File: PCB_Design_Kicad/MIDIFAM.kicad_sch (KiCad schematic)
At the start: 44 parts, among them IC1 DAC8562SDGSR, J1 PWR_IN, J10 midi, J2 ISP connector, U1 TL072, U2 MCP1703Ax-500xxDB, U5 6N137, U6 ATmega328-A

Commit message: better routing
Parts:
- added J11: back bottom, Connector_PinHeader_2.54mm:PinHeader_1x11_P2.54mm_Vertical, symbol Connector_Generic:Conn_01x11
- added J13: back top, Connector_PinHeader_2.54mm:PinHeader_1x07_P2.54mm_Vertical, symbol Connector_Generic:Conn_01x07
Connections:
- net GND: now also J11.11 (Pin_11), J13.7 (Pin_7)
- net adv_clock_b: now also J13.4 (Pin_4)
- net learn_sw_b: now also J11.5 (Pin_5)
- net led_a1_b: now also J11.7 (Pin_7)
- net led_a2_b: now also J11.8 (Pin_8)
- net led_b1_b: now also J11.4 (Pin_4)
- net led_b2_b: now also J11.3 (Pin_3)
- net led_cl1_b: now also J11.10 (Pin_10)
- net led_cl2_b: now also J11.9 (Pin_9)
- net seq_mode_sw_b: now also J13.3 (Pin_3)
- net sync_sw_b: now also J11.6 (Pin_6)
- net trig_a_b: now also J11.2 (Pin_2)
- net trig_b_b: now also J11.1 (Pin_1)
- net vel_a_b: now also J13.2 (Pin_2)
- net vel_b_b: now also J13.1 (Pin_1)
- net voct_a_b: now also J13.5 (Pin_5)
- net voct_b_b: now also J13.6 (Pin_6)
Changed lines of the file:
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@@
 	)
 	(label "led_cl2_b"
-		(at 116.84 78.74 180)
+		(at 121.92 58.42 180)
 		(fields_autoplaced yes)
 		(effects
@@
 	)
 	(label "trig_b_b"
-		(at 116.84 50.165 180)
+		(at 121.92 38.1 180)
 		(fields_autoplaced yes)
 		(effects
@@
 	)
 	(label "seq_mode_sw_b"
-		(at 116.84 81.28 180)
+		(at 121.92 81.915 180)
 		(fields_autoplaced yes)
 		(effects
@@
 	)
 	(label "learn_sw_b"
-		(at 116.84 31.75 180)
+		(at 121.92 48.26 180)
 		(fields_autoplaced yes)
 		(effects
@@
 	)
 	(label "sync_sw_b"
-		(at 116.84 29.21 180)
+		(at 121.92 50.8 180)
 		(fields_autoplaced yes)
 		(effects
@@
 	)
 	(label "led_a1_b"
-		(at 116.84 26.67 180)
+		(at 121.92 53.34 180)
 		(fields_autoplaced yes)
 		(effects
@@
 	)
 	(label "adv_clock_b"
-		(at 116.84 83.82 180)
+		(at 121.92 84.455 180)
 		(fields_autoplaced yes)
 		(effects
@@
 	)
 	(label "voct_b_b"
-		(at 116.84 55.245 180)
+		(at 121.92 89.535 180)
 		(fields_autoplaced yes)
 		(effects
@@
 	)
 	(label "led_b2_b"
-		(at 116.84 36.83 180)
+		(at 121.92 43.18 180)
 		(fields_autoplaced yes)
 		(effects
@@
 	)
 	(label "vel_b_b"
-		(at 116.84 62.865 180)
+		(at 121.92 76.835 180)
 		(fields_autoplaced yes)
 		(effects
@@
 	)
 	(label "trig_a_b"
-		(at 116.84 52.705 180)
+		(at 121.92 40.64 180)
 		(fields_autoplaced yes)
 		(effects
@@
 	)
 	(label "led_a2_b"
-		(at 116.84 24.13 180)
+		(at 121.92 55.88 180)
 		(fields_autoplaced yes)
 		(effects
@@
 	)
 	(label "vel_a_b"
-		(at 116.84 60.325 180)
+		(at 121.92 79.375 180)
 		(fields_autoplaced yes)
 		(effects
@@
 	)
 	(label "voct_a_b"
-		(at 116.84 57.785 180)
+		(at 121.92 86.995 180)
 		(fields_autoplaced yes)
 		(effects
@@
 	)
 	(label "led_b1_b"
-		(at 116.84 34.29 180)
+		(at 121.92 45.72 180)
 		(fields_autoplaced yes)
 		(effects
@@
 	)
 	(label "led_cl1_b"
-		(at 116.84 76.2 180)
+		(at 121.92 60.96 180)
 		(fields_autoplaced yes)
 		(effects
@@
 	(symbol
 		(lib_id "power:GND")
-		(at 116.84 65.405 0)
+		(at 121.92 92.075 0)
 		(unit 1)
 		(exclude_from_sim no)
@@
 		(dnp no)
 		(property "Reference" "#PWR033"
-			(at 116.84 71.755 0)
+			(at 121.92 98.425 0)
 			(effects
 				(font
@@
 		)
 		(property "Value" "GND"
-			(at 116.84 69.215 0)
+			(at 121.92 95.885 0)
 			(effects
 				(font
@@
 		)
 		(property "Footprint" ""
-			(at 116.84 65.405 0)
+			(at 121.92 92.075 0)
 			(effects
 				(font
@@
 		)
 		(property "Datasheet" ""
-			(at 116.84 65.405 0)
+			(at 121.92 92.075 0)
 			(effects
 				(font
@@
 		)
 		(property "Description" "Power symbol creates a global label with name \"GND\" , ground"
-			(at 116.84 65.405 0)
+			(at 121.92 92.075 0)
 			(effects
 				(font
@@
 	)
 	(symbol
+		(lib_id "Connector_Generic:Conn_01x07")
+		(at 127 84.455 0)
+		(unit 1)
+		(exclude_from_sim no)
+		(in_bom yes)
+		(on_board yes)
+		(dnp no)
+		(fields_autoplaced yes)
+		(property "Reference" "J13"
+			(at 129.54 83.1849 0)
+			(effects
+				(font
+					(size 1.27 1.27)
+				)
+				(justify left)
+			)
+		)
+		(property "Value" "back top"
+			(at 129.54 85.7249 0)
+			(effects
+				(font
+					(size 1.27 1.27)
+				)
+				(justify left)
+			)
+		)
+		(property "Footprint" "Connector_PinHeader_2.54mm:PinHeader_1x07_P2.54mm_Vertical"
+			(at 127 84.455 0)
+			(effects
+				(font
+					(size 1.27 1.27)
+				)
+				(hide yes)
+			)
+		)
+		(property "Datasheet" "~"
+			(at 127 84.455 0)
+			(effects
+				(font
+					(size 1.27 1.27)
+				)
+				(hide yes)
+			)
+		)
+		(property "Description" "Generic connector, single row, 01x07, script generated (kicad-library-utils/schlib/autogen/connector/)"
+			(at 127 84.455 0)
+			(effects
+				(font
+					(size 1.27 1.27)
+				)
+				(hide yes)
+			)
+		)
+		(pin "2"
+		)
+		(pin "1"
+		)
+		(pin "3"
+		)
+		(pin "6"
+		)
+		(pin "4"
+		)
+		(pin "5"
+		)
+		(pin "7"
+		)
+		(instances
+			(project ""
+				(path "/4d4d84f1-a7a8-42a8-95d1-cf69d5b591e2"
+					(reference "J13")
+					(unit 1)
+				)
+			)
+		)
+	)
+	(symbol
 		(lib_id "power:GND")
 		(at 208.28 144.78 0)
@@
 	)
 	(symbol
+		(lib_id "Connector_Generic:Conn_01x11")
+		(at 127 50.8 0)
+		(unit 1)
+		(exclude_from_sim no)
+		(in_bom yes)
+		(on_board yes)
+		(dnp no)
+		(fields_autoplaced yes)
+		(property "Reference" "J11"
+			(at 129.54 49.5299 0)
+			(effects
+				(font
+					(size 1.27 1.27)
+				)
+				(justify left)
+			)
+		)
+		(property "Value" "back bottom"
+			(at 129.54 52.0699 0)
+			(effects
+				(font
+					(size 1.27 1.27)
+				)
+				(justify left)
+			)
+		)
+		(property "Footprint" "Connector_PinHeader_2.54mm:PinHeader_1x11_P2.54mm_Vertical"
+			(at 127 50.8 0)
+			(effects
+				(font
+					(size 1.27 1.27)
+				)
+				(hide yes)
+			)
+		)
+		(property "Datasheet" "~"
+			(at 127 50.8 0)
+			(effects
+				(font
+					(size 1.27 1.27)
+				)
+				(hide yes)
+			)
+		)
+		(property "Description" "Generic connector, single row, 01x11, script generated (kicad-library-utils/schlib/autogen/connector/)"
+			(at 127 50.8 0)
+			(effects
+				(font
+					(size 1.27 1.27)
+				)
+				(hide yes)
+			)
+		)
+		(pin "6"
+		)
+		(pin "10"
+		)
+		(pin "9"
+		)
+		(pin "1"
+		)
+		(pin "5"
+		)
+		(pin "8"
+		)
+		(pin "11"
+		)
+		(pin "3"
+		)
+		(pin "7"
+		)
+		(pin "2"
+		)
+		(pin "4"
+		)
+		(instances
+			(project ""
+				(path "/4d4d84f1-a7a8-42a8-95d1-cf69d5b591e2"
+					(reference "J11")
+					(unit 1)
+				)
+			)
+		)
+	)
+	(symbol
 		(lib_id "Regulator_Linear:MCP1703Ax-500xxDB")
 		(at 92.075 173.355 270)
@@
 	(symbol
 		(lib_id "power:GND")
-		(at 116.84 39.37 0)
+		(at 121.92 63.5 0)
 		(unit 1)
 		(exclude_from_sim no)
@@
 		(dnp no)
 		(property "Reference" "#PWR034"
-			(at 116.84 45.72 0)
+			(at 121.92 69.85 0)
 			(effects
 				(font
@@
 		)
 		(property "Value" "GND"
-			(at 116.84 43.18 0)
+			(at 121.92 67.31 0)
 			(effects
 				(font
@@
 		)
 		(property "Footprint" ""
-			(at 116.84 39.37 0)
+			(at 121.92 63.5 0)
 			(effects
 				(font
@@
 		)
 		(property "Datasheet" ""
-			(at 116.84 39.37 0)
+			(at 121.92 63.5 0)
 			(effects
 				(font
@@
 		)
 		(property "Description" "Power symbol creates a global label with name \"GND\" , ground"
-			(at 116.84 39.37 0)
+			(at 121.92 63.5 0)
 			(effects
 				(font
@@
 					(unit 1)
 				)
-			)
-		)
-	)
-	(symbol
-		(lib_id "power:GND")
-		(at 116.84 86.36 0)
-		(unit 1)
-		(exclude_from_sim no)
-		(in_bom yes)
-		(on_board yes)
-		(dnp no)
-		(property "Reference" "#PWR032"
-			(at 116.84 92.71 0)
-			(effects
-				(font
-					(size 1.27 1.27)
-				)
-				(hide yes)
-			)
-		)
-		(property "Value" "GND"
-			(at 116.84 90.17 0)
-			(effects
-				(font
-					(size 1.27 1.27)
-				)
-			)
-		)
-		(property "Footprint" ""
-			(at 116.84 86.36 0)
-			(effects
-				(font
-					(size 1.27 1.27)
-				)
-				(hide yes)
-			)
-		)
-		(property "Datasheet" ""
-			(at 116.84 86.36 0)
-			(effects
-				(font
-					(size 1.27 1.27)
-				)
-				(hide yes)
-			)
-		)
-		(property "Description" "Power symbol creates a global label with name \"GND\" , ground"
-			(at 116.84 86.36 0)
-			(effects
-				(font
-					(size 1.27 1.27)
-				)
-				(hide yes)
-			)
-		)
-		(pin "1"
-		)
-		(instances
-			(project "MIDIFAM"
-				(path "/4d4d84f1-a7a8-42a8-95d1-cf69d5b591e2"
-					(reference "#PWR032")
-					(unit 1)
-				)

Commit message: ready for schematic review
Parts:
- removed C4, C5: 1u, Capacitor_SMD:C_0603_1608Metric, symbol Device:C_Polarized_Small
- added C18, C19: 18p, Capacitor_SMD:C_0603_1608Metric, symbol Device:C_Small
- added D7: 1N4148, Diode_SMD:D_SOD-323_HandSoldering, symbol Device:D_Small
- added R16, R17: 47k, Resistor_SMD:R_0603_1608Metric_Pad0.98x0.95mm_HandSolder, symbol Device:R_Small
- added R18, R19: 1k, Resistor_SMD:R_0603_1608Metric_Pad0.98x0.95mm_HandSolder, symbol Device:R_Small
- R1, R3: value ? -> 240k
- R2, R4: value ? -> 47k
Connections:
- net 5V: now also D7.1 (K)
- net DAC_OUT_A: now also R2.2; no longer U1.5 (+)
- net DAC_OUT_B: now also R4.2; no longer U1.3 (+)
- net GND: now also R17.1; no longer R2.1, R4.1
- net RESET: now also D7.2 (A)
- net VREF_DAC: now also R16.2
- net voct_a_b: now also R1.1, R18.1; no longer R1.2, U1.7
- net voct_b_b: now also R3.1, R19.1; no longer R3.2, U1.1
- new net: C19.1, R3.2, R4.1, U1.2 (-)
- new net: C18.2, R18.2, U1.7
- new net: C18.1, R1.2, R2.1, U1.6 (-)
- new net: C19.2, R19.2, U1.1
- new net VREF/2: R16.1, R17.2, U1.3 (+), U1.5 (+)
- no-connect marks 4 -> 6
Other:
- moved on the sheet: C17, IC1, R10, R11, R12, R13, R14, U1A, U1B

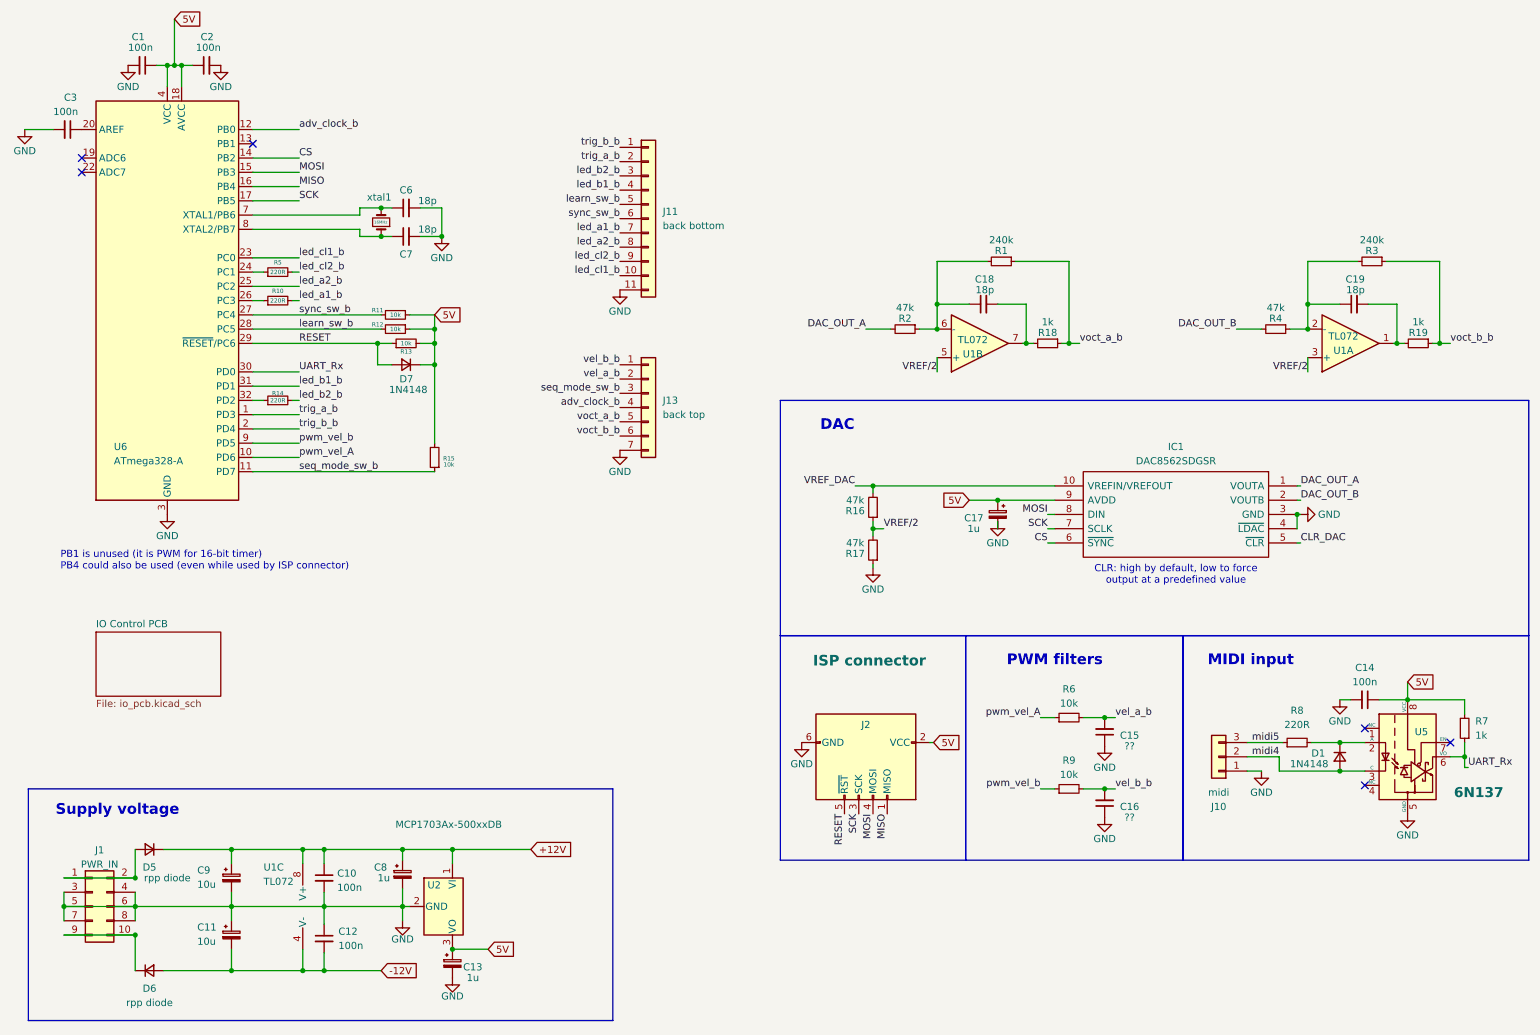
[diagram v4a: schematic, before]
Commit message: op amps for velocity!
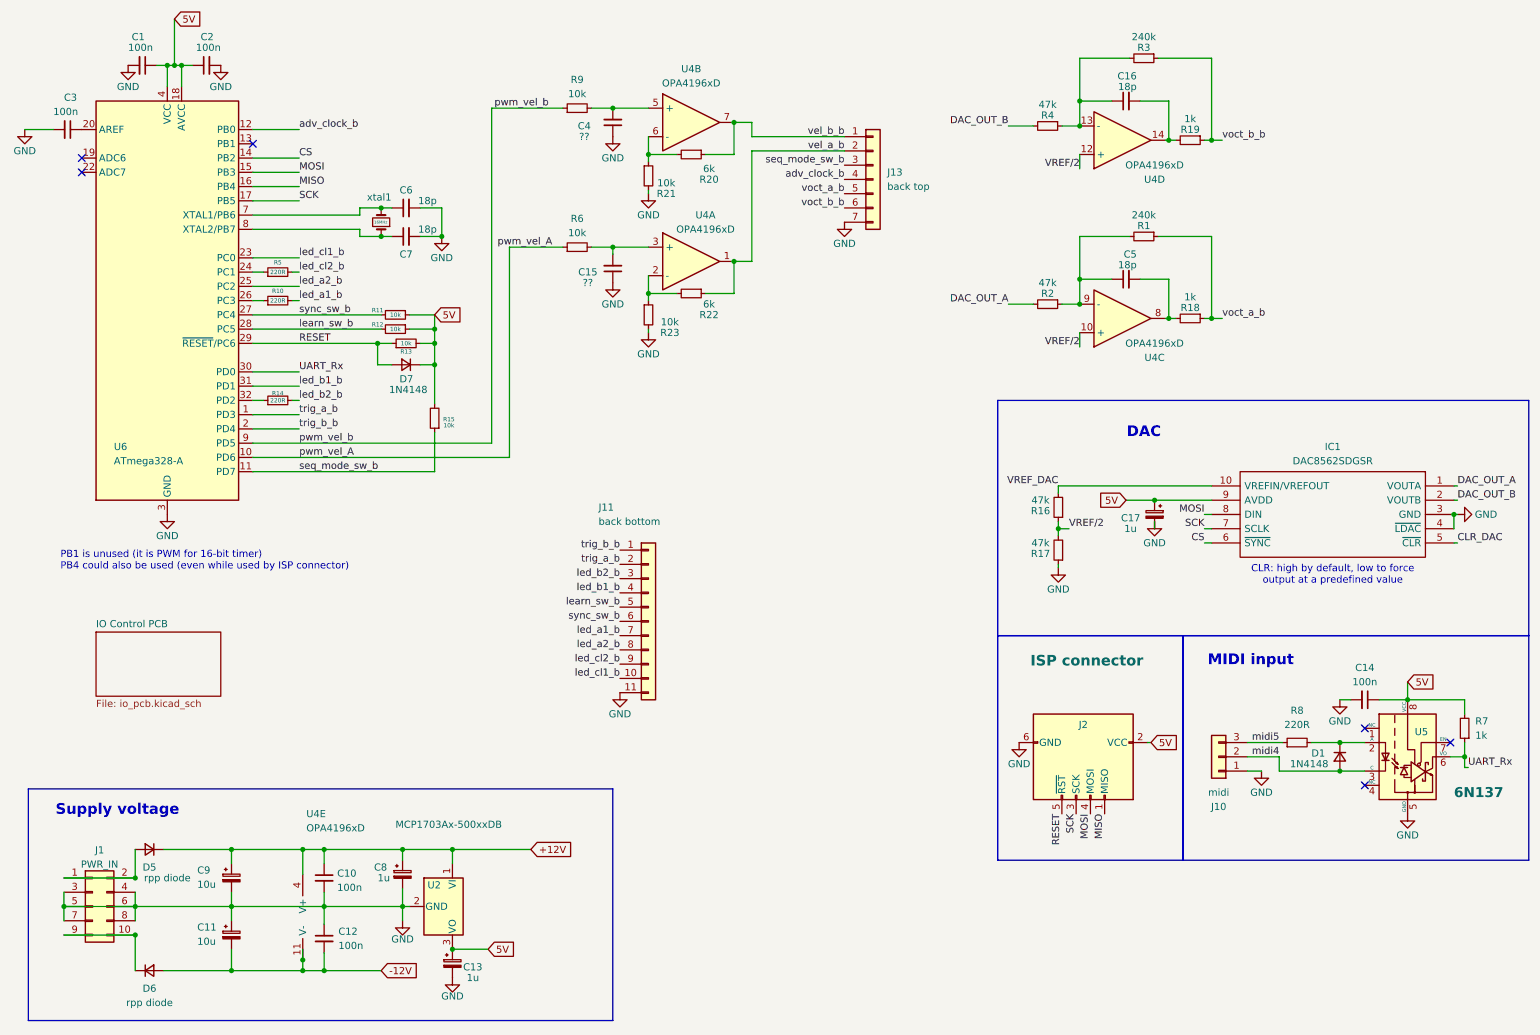
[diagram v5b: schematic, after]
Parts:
- removed C18, C19: 18p, Capacitor_SMD:C_0603_1608Metric, symbol Device:C_Small
- removed U1: TL072, Package_SO:SOIC-8_3.9x4.9mm_P1.27mm, symbol Amplifier_Operational:TL072
- added C4: ??, Capacitor_SMD:C_0603_1608Metric, symbol Device:C_Small
- added C5: 18p, Capacitor_SMD:C_0603_1608Metric, symbol Device:C_Small
- added R20, R22: 6k, Resistor_SMD:R_0603_1608Metric_Pad0.98x0.95mm_HandSolder, symbol Device:R_Small
- added R21, R23: 10k, Resistor_SMD:R_0603_1608Metric_Pad0.98x0.95mm_HandSolder, symbol Device:R_Small
- added U4: OPA4196xD, Package_SO:SOIC-14_3.9x8.7mm_P1.27mm, symbol Amplifier_Operational:OPA4196xD
- C16: value ?? -> 18p
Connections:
- net +12V: now also U4.4 (V+)
- net -12V: now also U4.11 (V-)
- net GND: now also C4.1, R21.2, R23.2; no longer C16.1
- net VREF/2: now also U4.10 (+), U4.12 (+)
- net vel_a_b: now also R22.1, U4.1; no longer C15.2, R6.2
- net vel_b_b: now also R20.1, U4.7; no longer C16.2, R9.2
- net at R3.2, R4.1: now also C16.1, U4.13 (-)
- net at R18.2: now also C5.2, U4.8
- net at R1.2, R2.1: now also C5.1, U4.9 (-)
- net at R19.2: now also C16.2, U4.14
- new net: R22.2, R23.1, U4.2 (-)
- new net: C15.2, R6.2, U4.3 (+)
- new net: R20.2, R21.1, U4.6 (-)
- new net: C4.2, R9.2, U4.5 (+)
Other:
- note removed: "PWM filters"
- moved on the sheet: C15, C17, IC1, J11, J13, J2, R15, R16, R17, R6

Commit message: adding to BOM
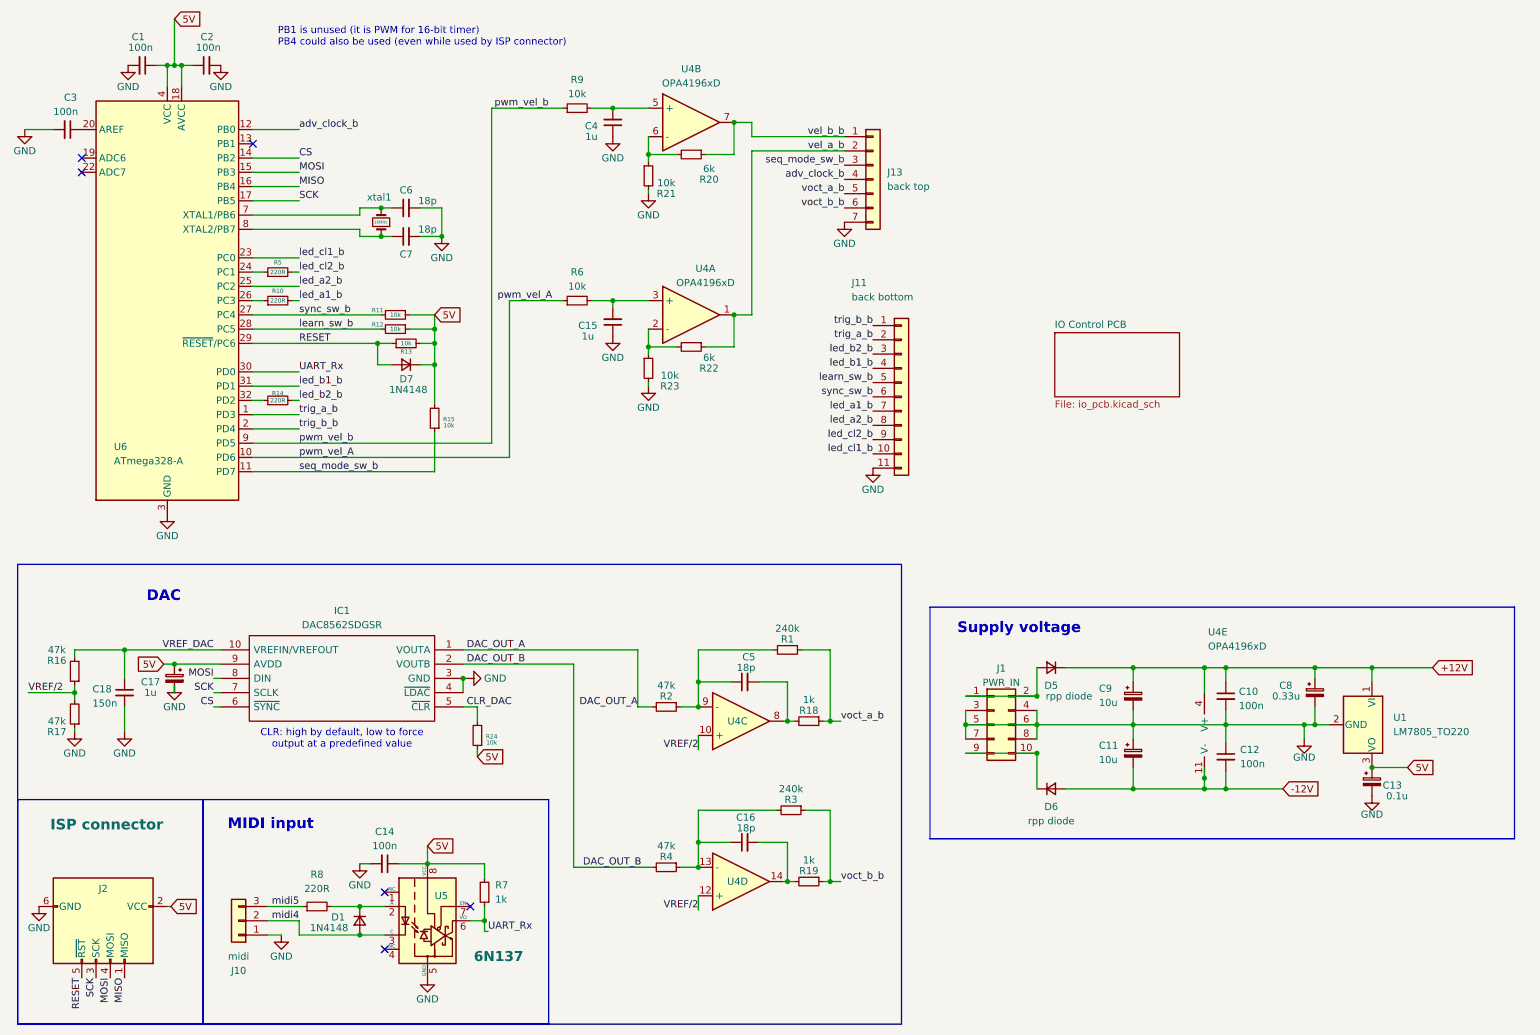
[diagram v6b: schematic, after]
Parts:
- removed U2: MCP1703Ax-500xxDB, Package_TO_SOT_SMD:SOT-223-3_TabPin2, symbol Regulator_Linear:MCP1703Ax-500xxDB
- added C18: 150n, Capacitor_SMD:C_0603_1608Metric, symbol Device:C_Small
- added R24: 10k, Resistor_SMD:R_0603_1608Metric_Pad0.98x0.95mm_HandSolder, symbol Device:R_Small
- added U1: LM7805_TO220, Package_TO_SOT_THT:TO-220-3_Vertical, symbol Regulator_Linear:LM7805_TO220
- C1, C10, C12, C14, C2, C3: LCSC (none) -> C143639
- C11, C9: footprint Capacitor_SMD:CP_Elec_5x5.3 -> Capacitor_SMD:CP_Elec_5x5.4; LCSC (none) -> C336586
- C13: value 1u -> 0.1u; LCSC (none) -> C2691405
- C15, C4: value ?? -> 1u; LCSC (none) -> C2691405
- C16, C5, C6, C7: LCSC (none) -> C184235
- C17: LCSC (none) -> C2691405
- C8: value 1u -> 0.33u; LCSC (none) -> C2691405
- D1, D7: LCSC (none) -> C108805
- D5, D6: LCSC (none) -> C688896
- IC1: LCSC (none) -> C127965
- R1, R3: LCSC (none) -> C407611
- R10, R14, R5, R8: LCSC (none) -> C365121
- R11, R12, R13, R15, R21, R23, R6, R9: LCSC (none) -> C845630
- R16, R17, R2, R4: LCSC (none) -> C2907042
- R18, R19, R7: LCSC (none) -> C2758735
- U4: footprint Package_SO:SOIC-14_3.9x8.7mm_P1.27mm -> Package_SO:TSSOP-14_4.4x5mm_P0.65mm; LCSC (none) -> C2873620; Price (single) (none) -> $0.88
- U5: LCSC (none) -> C92651
- U6: LCSC (none) -> C14877
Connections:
- net +12V: now also U1.1 (VI)
- net 5V: now also R24.1, U1.3 (VO)
- net CLR_DAC: now also R24.2
- net GND: now also C18.2, U1.2 (GND)
- net VREF_DAC: now also C18.1
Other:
- moved on the sheet: C10, C11, C12, C13, C14, C15, C16, C17, C5, C8, C9, D1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
